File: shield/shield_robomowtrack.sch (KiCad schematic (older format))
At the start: 30 parts

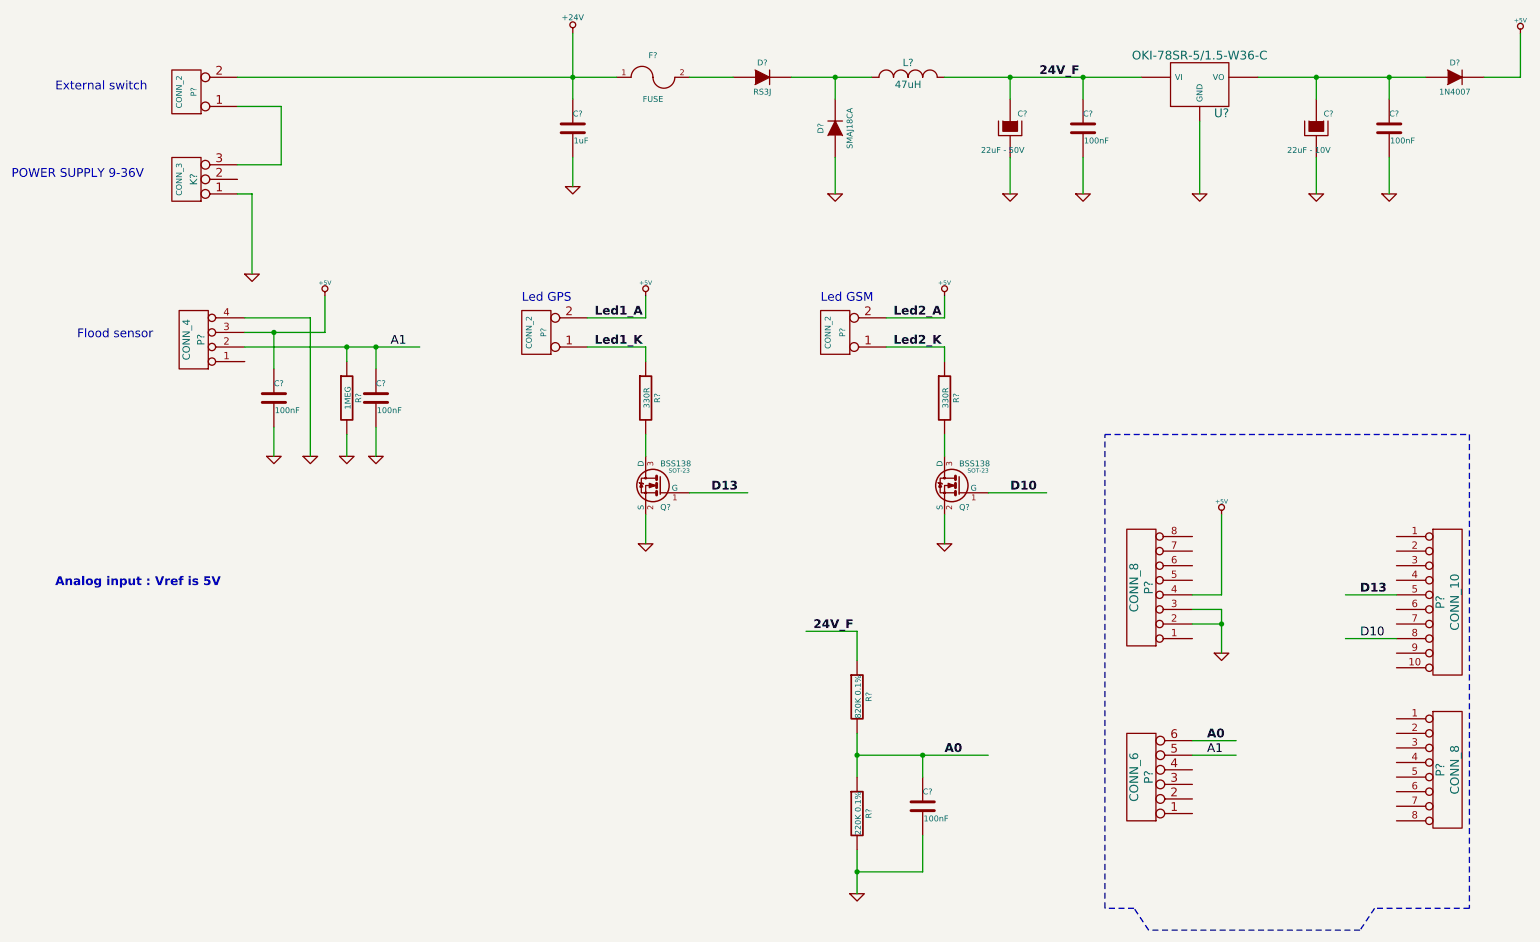
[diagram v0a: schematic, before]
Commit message: Shield : - add PDF schematic - add datasheet - add BOM - add netlist and raw BOM
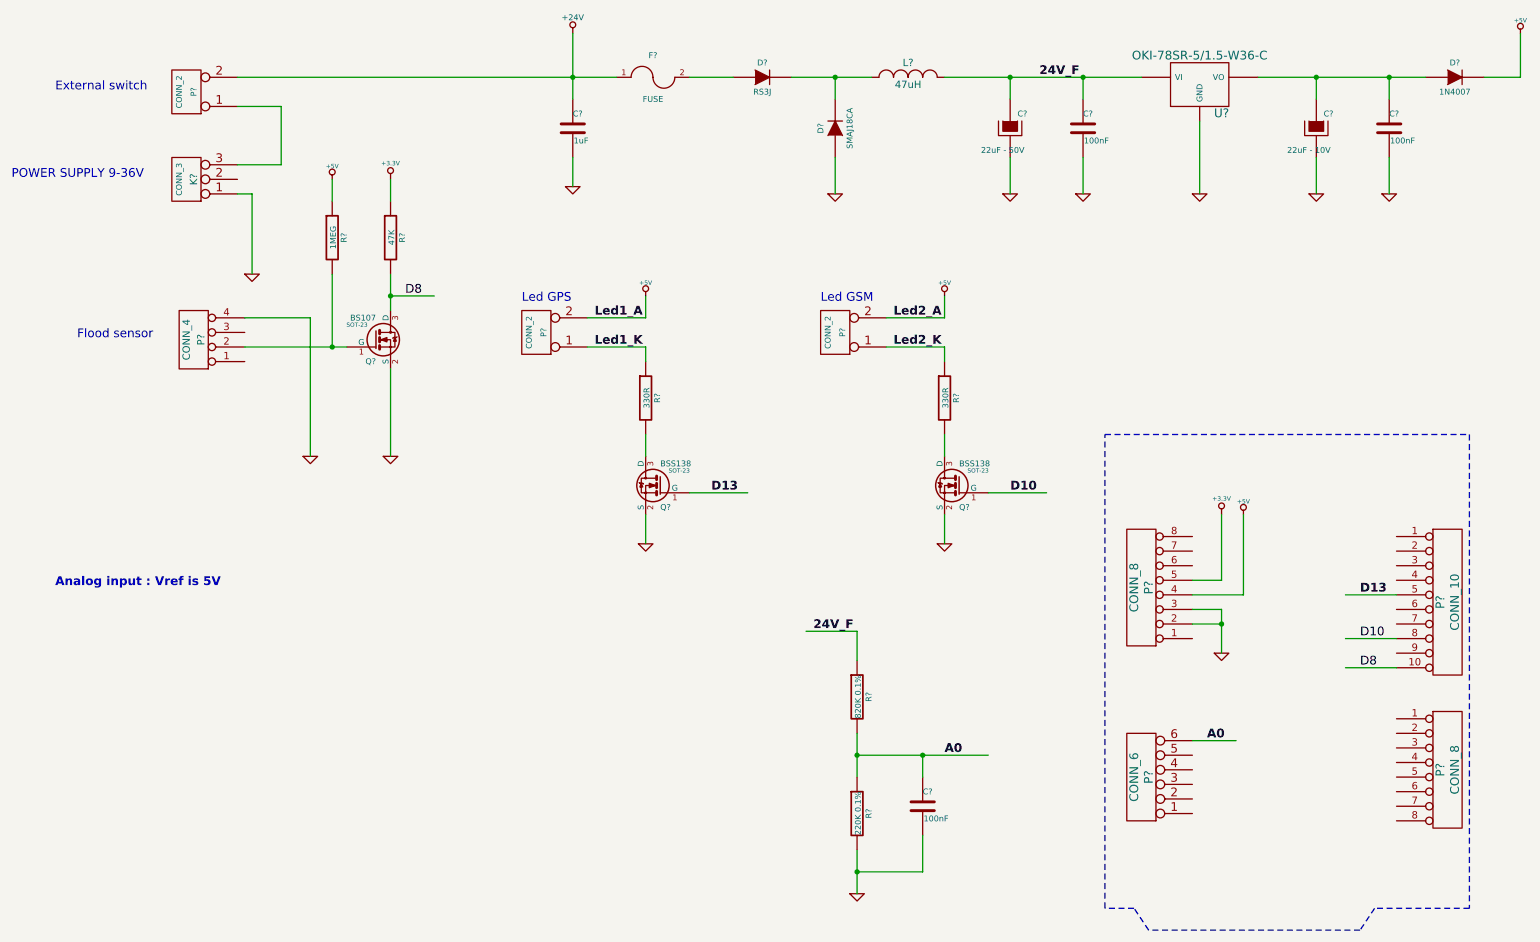
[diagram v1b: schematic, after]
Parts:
- removed C? (x2): 100nF, ~, symbol C
- removed R?: 1MEG, ~, symbol R
- added Q?: BS107, SOT-23, symbol BSS138
- added R?: 1MEG, ~, symbol R
- added R?: 47K, ~, symbol R
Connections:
- net labels added: +3.3V, D8
- net labels removed: A1
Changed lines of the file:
@@
 Sheet 1 1
 Title ""
-Date "2 feb 2015"
+Date "10 mar 2015"
 Rev ""
 Comp ""
@@
 12 48 00 00 00 00 00 00 00 00 ED 02 09 24 00 00 00 00 00 00 00 80 76 81 04 12 00 00 00 00 00 00
 00 3A EC 15 6D 00 00 00 08 49 44 41 54 40 BB FC 1F EA CD 97 87 08 2E F3 10 00 00 00 00 49 45 4E
-44 AE 42 60 82 0B $EndBitmap
+44 AE 42 60 82 2A $EndBitmap
 EndData
 $EndBitmap
@@
 Connection ~ 8800 4800
 Wire Wire Line
-	8600 4600 8800 4600
-Wire Wire Line
-	8800 4600 8800 4050
+	8600 4600 8950 4600
 $Comp
 L +5V #PWR?
 U 1 1 54B83500
-P 8800 4050
-F 0 "#PWR?" H 8800 4140 20  0001 C CNN
-F 1 "+5V" H 8800 4140 30  0000 C CNN
-F 2 "" H 8800 4050 60  0000 C CNN
-F 3 "" H 8800 4050 60  0000 C CNN
-	1    8800 4050
+P 8950 4050
+F 0 "#PWR?" H 8950 4140 20  0001 C CNN
+F 1 "+5V" H 8950 4140 30  0000 C CNN
+F 2 "" H 8950 4050 60  0000 C CNN
+F 3 "" H 8950 4050 60  0000 C CNN
+	1    8950 4050
 	1    0    0    -1
 $EndComp
@@
 Wire Wire Line
 	2150 1850 2050 1850
-$Comp
-L GND #PWR?
-U 1 1 54C0F956
-P 2800 3650
-F 0 "#PWR?" H 2800 3650 30  0001 C CNN
-F 1 "GND" H 2800 3580 30  0001 C CNN
-F 2 "" H 2800 3650 60  0000 C CNN
-F 3 "" H 2800 3650 60  0000 C CNN
-	1    2800 3650
-	1    0    0    -1
-$EndComp
-$Comp
-L R R?
-U 1 1 54C0F95D
-P 2800 3250
-F 0 "R?" V 2880 3250 40  0000 C CNN
-F 1 "1MEG" V 2807 3251 40  0000 C CNN
-F 2 "~" V 2730 3250 30  0000 C CNN
-F 3 "~" H 2800 3250 30  0000 C CNN
-	1    2800 3250
-	1    0    0    -1
-$EndComp
-Wire Wire Line
-	2800 3650 2800 3500
-Wire Wire Line
-	2800 2900 2800 3000
-Wire Wire Line
-	2650 2800 2650 2550
-$Comp
-L +5V #PWR?
-U 1 1 54C0F96A
-P 2650 2550
-F 0 "#PWR?" H 2650 2640 20  0001 C CNN
-F 1 "+5V" H 2650 2640 30  0000 C CNN
-F 2 "" H 2650 2550 60  0000 C CNN
-F 3 "" H 2650 2550 60  0000 C CNN
-	1    2650 2550
-	1    0    0    -1
-$EndComp
-Wire Wire Line
-	8600 5700 8900 5700
-Text Label 8700 5700 0    60   ~ 0
-A1
-Text Label 3100 2900 0    60   ~ 0
-A1
-$Comp
-L C C?
-U 1 1 54C0FA0B
-P 3000 3250
-F 0 "C?" H 3000 3350 40  0000 L CNN
-F 1 "100nF" H 3006 3165 40  0000 L CNN
-F 2 "~" H 3038 3100 30  0000 C CNN
-F 3 "~" H 3000 3250 60  0000 C CNN
-	1    3000 3250
-	1    0    0    -1
-$EndComp
-$Comp
-L GND #PWR?
-U 1 1 54C0FA11
-P 3000 3650
-F 0 "#PWR?" H 3000 3650 30  0001 C CNN
-F 1 "GND" H 3000 3580 30  0001 C CNN
-F 2 "" H 3000 3650 60  0000 C CNN
-F 3 "" H 3000 3650 60  0000 C CNN
-	1    3000 3650
-	1    0    0    -1
-$EndComp
-Wire Wire Line
-	3000 3050 3000 2900
-Connection ~ 3000 2900
-Wire Wire Line
-	3000 3450 3000 3650
-Wire Wire Line
-	2100 2900 3300 2900
 Text Notes 500  1750 0    60   ~ 0
 POWER SUPPLY 9-36V
@@
 Wire Wire Line
 	2550 2700 2550 3650
-Wire Wire Line
-	2100 2800 2650 2800
-$Comp
-L C C?
-U 1 1 54C0FEA9
-P 2300 3250
-F 0 "C?" H 2300 3350 40  0000 L CNN
-F 1 "100nF" H 2306 3165 40  0000 L CNN
-F 2 "~" H 2338 3100 30  0000 C CNN
-F 3 "~" H 2300 3250 60  0000 C CNN
-	1    2300 3250
-	1    0    0    -1
-$EndComp
-$Comp
-L GND #PWR?
-U 1 1 54C0FEAF
-P 2300 3650
-F 0 "#PWR?" H 2300 3650 30  0001 C CNN
-F 1 "GND" H 2300 3580 30  0001 C CNN
-F 2 "" H 2300 3650 60  0000 C CNN
-F 3 "" H 2300 3650 60  0000 C CNN
-	1    2300 3650
-	1    0    0    -1
-$EndComp
-Wire Wire Line
-	2300 3450 2300 3650
-Wire Wire Line
-	2300 2800 2300 3050
-Connection ~ 2300 2800
 $Comp
 L INDUCTOR_SMALL L?
@@
 Text Notes 800  1150 0    60   ~ 0
 External switch
-Connection ~ 2800 2900
 Wire Wire Line
 	4850 2900 4450 2900
@@
 Text Label 9750 4900 0    60   ~ 0
 D10
+$Comp
+L BSS138 Q?
+U 1 1 54FE0B5F
+P 3000 2850
+F 0 "Q?" H 3000 2701 40  0000 R CNN
+F 1 "BS107" H 3000 3000 40  0000 R CNN
+F 2 "SOT-23" H 2870 2952 29  0000 C CNN
+F 3 "~" H 3000 2850 60  0000 C CNN
+	1    3000 2850
+	1    0    0    -1
+$EndComp
+$Comp
+L GND #PWR?
+U 1 1 54FE0CE7
+P 3100 3650
+F 0 "#PWR?" H 3100 3650 30  0001 C CNN
+F 1 "GND" H 3100 3580 30  0001 C CNN
+F 2 "" H 3100 3650 60  0000 C CNN
+F 3 "" H 3100 3650 60  0000 C CNN
+	1    3100 3650
+	1    0    0    -1
+$EndComp
+Wire Wire Line
+	3100 3650 3100 3050
+Wire Wire Line
+	3100 2400 3100 2650
+Wire Wire Line
+	3100 2550 3400 2550
+Text Label 3200 2550 0    60   ~ 0
+D8
+Wire Wire Line
+	2800 2900 2100 2900
+Connection ~ 2700 2900
+$Comp
+L R R?
+U 1 1 54FF4D16
+P 3100 2150
+F 0 "R?" V 3180 2150 40  0000 C CNN
+F 1 "47K" V 3107 2151 40  0000 C CNN
+F 2 "~" V 3030 2150 30  0000 C CNN
+F 3 "~" H 3100 2150 30  0000 C CNN
+	1    3100 2150
+	1    0    0    -1
+$EndComp
+$Comp
+L +5V #PWR?
+U 1 1 54FF4D1C
+P 2700 1750
+F 0 "#PWR?" H 2700 1840 20  0001 C CNN
+F 1 "+5V" H 2700 1840 30  0000 C CNN
+F 2 "" H 2700 1750 60  0000 C CNN
+F 3 "" H 2700 1750 60  0000 C CNN
+	1    2700 1750
+	1    0    0    -1
+$EndComp
+Wire Wire Line
+	2700 1900 2700 1750
+Connection ~ 3100 2550
+$Comp
+L R R?
+U 1 1 54FF4C5E
+P 2700 2150
+F 0 "R?" V 2780 2150 40  0000 C CNN
+F 1 "1MEG" V 2707 2151 40  0000 C CNN
+F 2 "~" V 2630 2150 30  0000 C CNN
+F 3 "~" H 2700 2150 30  0000 C CNN
+	1    2700 2150
+	1    0    0    -1
+$EndComp
+Wire Wire Line
+	3100 1900 3100 1750
+Wire Wire Line
+	2700 2400 2700 2900
+Wire Wire Line
+	8950 4600 8950 4050
+$Comp
+L +3.3V #PWR?
+U 1 1 54FF507D
+P 8800 4050
+F 0 "#PWR?" H 8800 4010 30  0001 C CNN
+F 1 "+3.3V" H 8800 4160 30  0000 C CNN
+F 2 "" H 8800 4050 60  0000 C CNN
+F 3 "" H 8800 4050 60  0000 C CNN
+	1    8800 4050
+	1    0    0    -1
+$EndComp
+Wire Wire Line
+	8800 4050 8800 4500
+Wire Wire Line
+	8800 4500 8600 4500
+$Comp
+L +3.3V #PWR?
+U 1 1 54FF50E0
+P 3100 1750
+F 0 "#PWR?" H 3100 1710 30  0001 C CNN
+F 1 "+3.3V" H 3100 1860 30  0000 C CNN
+F 2 "" H 3100 1750 60  0000 C CNN
+F 3 "" H 3100 1750 60  0000 C CNN
+	1    3100 1750
+	1    0    0    -1
+$EndComp
+Wire Wire Line
+	10000 5100 9650 5100
+Text Label 9750 5100 0    60   ~ 0
+D8
 $EndSCHEMATC

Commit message: change voltage input conversion coef
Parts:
- R?: value 820K 0.1% -> 82K 0.1%
- R?: value 220K 0.1% -> 22K 0.1%
- R?: value 1MEG -> 4.7MEG
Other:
- moved on the sheet: R?
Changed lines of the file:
@@
 Sheet 1 1
 Title ""
-Date "10 mar 2015"
+Date "1 apr 2015"
 Rev ""
 Comp ""
@@
 12 48 00 00 00 00 00 00 00 00 ED 02 09 24 00 00 00 00 00 00 00 80 76 81 04 12 00 00 00 00 00 00
 00 3A EC 15 6D 00 00 00 08 49 44 41 54 40 BB FC 1F EA CD 97 87 08 2E F3 10 00 00 00 00 49 45 4E
-44 AE 42 60 82 2A $EndBitmap
+44 AE 42 60 82 A3 $EndBitmap
 EndData
 $EndBitmap
@@
 P 6300 5300
 F 0 "R?" V 6380 5300 40  0000 C CNN
-F 1 "820K 0.1%" V 6307 5301 40  0000 C CNN
+F 1 "82K 0.1%" V 6307 5301 40  0000 C CNN
 F 2 "~" V 6230 5300 30  0000 C CNN
 F 3 "~" H 6300 5300 30  0000 C CNN
@@
 P 6300 6100
 F 0 "R?" V 6380 6100 40  0000 C CNN
-F 1 "220K 0.1%" V 6307 6101 40  0000 C CNN
+F 1 "22K 0.1%" V 6307 6101 40  0000 C CNN
 F 2 "~" V 6230 6100 30  0000 C CNN
 F 3 "~" H 6300 6100 30  0000 C CNN
@@
 	-1   0    0    1
 $EndComp
-$Comp
-L GND #PWR?
-U 1 1 54C0FCE8
-P 2550 3650
-F 0 "#PWR?" H 2550 3650 30  0001 C CNN
-F 1 "GND" H 2550 3580 30  0001 C CNN
-F 2 "" H 2550 3650 60  0000 C CNN
-F 3 "" H 2550 3650 60  0000 C CNN
-	1    2550 3650
-	1    0    0    -1
-$EndComp
 Wire Wire Line
 	2100 2700 2550 2700
-Wire Wire Line
-	2550 2700 2550 3650
 $Comp
 L INDUCTOR_SMALL L?
@@
 	1    0    0    -1
 $EndComp
-$Comp
-L +5V #PWR?
-U 1 1 54FF4D1C
-P 2700 1750
-F 0 "#PWR?" H 2700 1840 20  0001 C CNN
-F 1 "+5V" H 2700 1840 30  0000 C CNN
-F 2 "" H 2700 1750 60  0000 C CNN
-F 3 "" H 2700 1750 60  0000 C CNN
-	1    2700 1750
-	1    0    0    -1
-$EndComp
-Wire Wire Line
-	2700 1900 2700 1750
 Connection ~ 3100 2550
 $Comp
 L R R?
 U 1 1 54FF4C5E
-P 2700 2150
-F 0 "R?" V 2780 2150 40  0000 C CNN
-F 1 "1MEG" V 2707 2151 40  0000 C CNN
-F 2 "~" V 2630 2150 30  0000 C CNN
-F 3 "~" H 2700 2150 30  0000 C CNN
-	1    2700 2150
+P 2700 3300
+F 0 "R?" V 2780 3300 40  0000 C CNN
+F 1 "4.7MEG" V 2707 3301 40  0000 C CNN
+F 2 "~" V 2630 3300 30  0000 C CNN
+F 3 "~" H 2700 3300 30  0000 C CNN
+	1    2700 3300
 	1    0    0    -1
 $EndComp
@@
 	3100 1900 3100 1750
 Wire Wire Line
-	2700 2400 2700 2900
-Wire Wire Line
 	8950 4600 8950 4050
 $Comp
@@
 Text Label 9750 5100 0    60   ~ 0
 D8
+$Comp
+L GND #PWR?
+U 1 1 55008BE3
+P 2700 3650
+F 0 "#PWR?" H 2700 3650 30  0001 C CNN
+F 1 "GND" H 2700 3580 30  0001 C CNN
+F 2 "" H 2700 3650 60  0000 C CNN
+F 3 "" H 2700 3650 60  0000 C CNN
+	1    2700 3650
+	1    0    0    -1
+$EndComp
+Wire Wire Line
+	2700 3650 2700 3550
+Wire Wire Line
+	2700 3050 2700 2900
+$Comp
+L +5V #PWR?
+U 1 1 55008C94
+P 2550 2400
+F 0 "#PWR?" H 2550 2490 20  0001 C CNN
+F 1 "+5V" H 2550 2490 30  0000 C CNN
+F 2 "" H 2550 2400 60  0000 C CNN
+F 3 "" H 2550 2400 60  0000 C CNN
+	1    2550 2400
+	1    0    0    -1
+$EndComp
+Wire Wire Line
+	2550 2700 2550 2400
 $EndSCHEMATC

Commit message: add timeout while downloading http header add some message when firmware update
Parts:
- added 1N4148W: DIODE, ~, symbol DIODE
- added R?: 1K, ~, symbol R
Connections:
- wire segments 67 -> 68
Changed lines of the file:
@@
 Sheet 1 1
 Title ""
-Date "1 apr 2015"
+Date "1 may 2015"
 Rev ""
 Comp ""
@@
 12 48 00 00 00 00 00 00 00 00 ED 02 09 24 00 00 00 00 00 00 00 80 76 81 04 12 00 00 00 00 00 00
 00 3A EC 15 6D 00 00 00 08 49 44 41 54 40 BB FC 1F EA CD 97 87 08 2E F3 10 00 00 00 00 49 45 4E
-44 AE 42 60 82 A3 $EndBitmap
+44 AE 42 60 82 CD $EndBitmap
 EndData
 $EndBitmap
@@
 $EndComp
 Wire Wire Line
-	2100 2700 2550 2700
+	2100 2700 2700 2700
 $Comp
 L INDUCTOR_SMALL L?
@@
 L +5V #PWR?
 U 1 1 55008C94
-P 2550 2400
-F 0 "#PWR?" H 2550 2490 20  0001 C CNN
-F 1 "+5V" H 2550 2490 30  0000 C CNN
-F 2 "" H 2550 2400 60  0000 C CNN
-F 3 "" H 2550 2400 60  0000 C CNN
-	1    2550 2400
+P 2700 1650
+F 0 "#PWR?" H 2700 1740 20  0001 C CNN
+F 1 "+5V" H 2700 1740 30  0000 C CNN
+F 2 "" H 2700 1650 60  0000 C CNN
+F 3 "" H 2700 1650 60  0000 C CNN
+	1    2700 1650
 	1    0    0    -1
 $EndComp
+$Comp
+L DIODE 1N4148W
+U 1 1 55434122
+P 2700 1950
+F 0 "1N4148W" H 2700 2050 40  0000 C CNN
+F 1 "DIODE" H 2700 1850 40  0000 C CNN
+F 2 "~" H 2700 1950 60  0000 C CNN
+F 3 "~" H 2700 1950 60  0000 C CNN
+	1    2700 1950
+	0    1    1    0
+$EndComp
+$Comp
+L R R?
+U 1 1 5543412F
+P 2700 2450
+F 0 "R?" V 2780 2450 40  0000 C CNN
+F 1 "1K" V 2707 2451 40  0000 C CNN
+F 2 "~" V 2630 2450 30  0000 C CNN
+F 3 "~" H 2700 2450 30  0000 C CNN
+	1    2700 2450
+	1    0    0    -1
+$EndComp
+Wire Wire Line
+	2700 1650 2700 1750
 Wire Wire Line
-	2550 2700 2550 2400
+	2700 2150 2700 2200
 $EndSCHEMATC
